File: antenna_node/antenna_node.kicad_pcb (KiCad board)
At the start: 4 copper layers, 68 parts, among them P1 CONN_01X03, P2 CONN_01X03, P3 CONN_01X02, P4 CONN_02X08, P5 CONN_01X06, P6 CONN_01X03, SW1 SW_PUSH, SW2 SW_PUSH, U1 0896BM15A0001, U2 TC77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

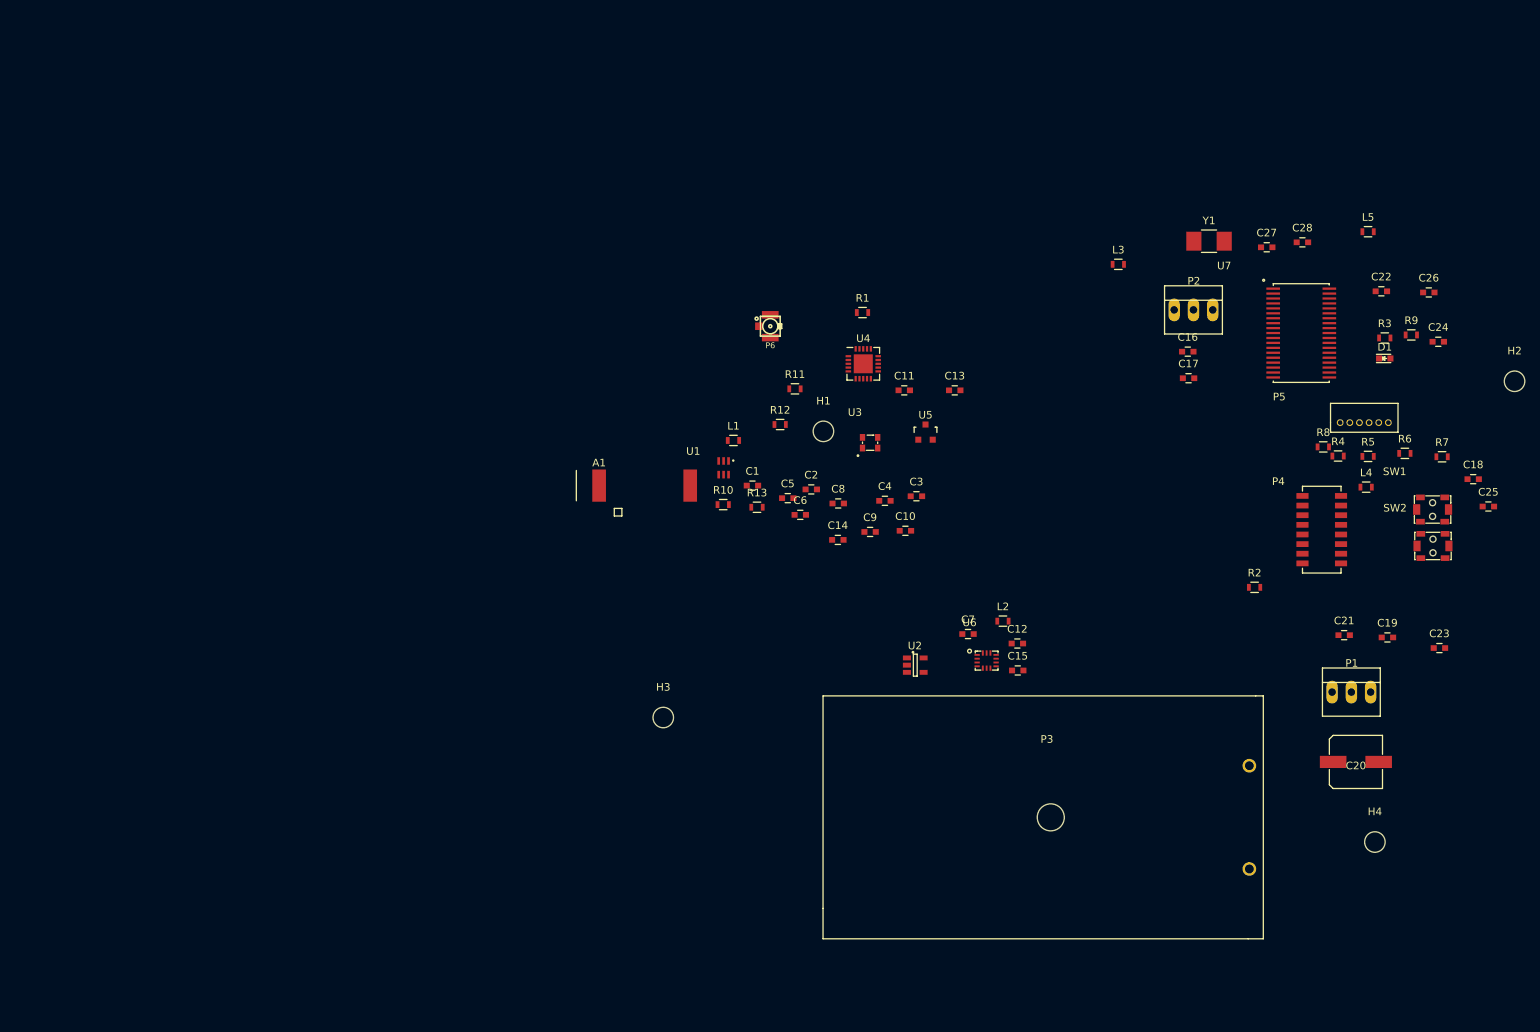
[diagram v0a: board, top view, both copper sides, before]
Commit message: finished initial compomnent placement, added rf shield and enclosure
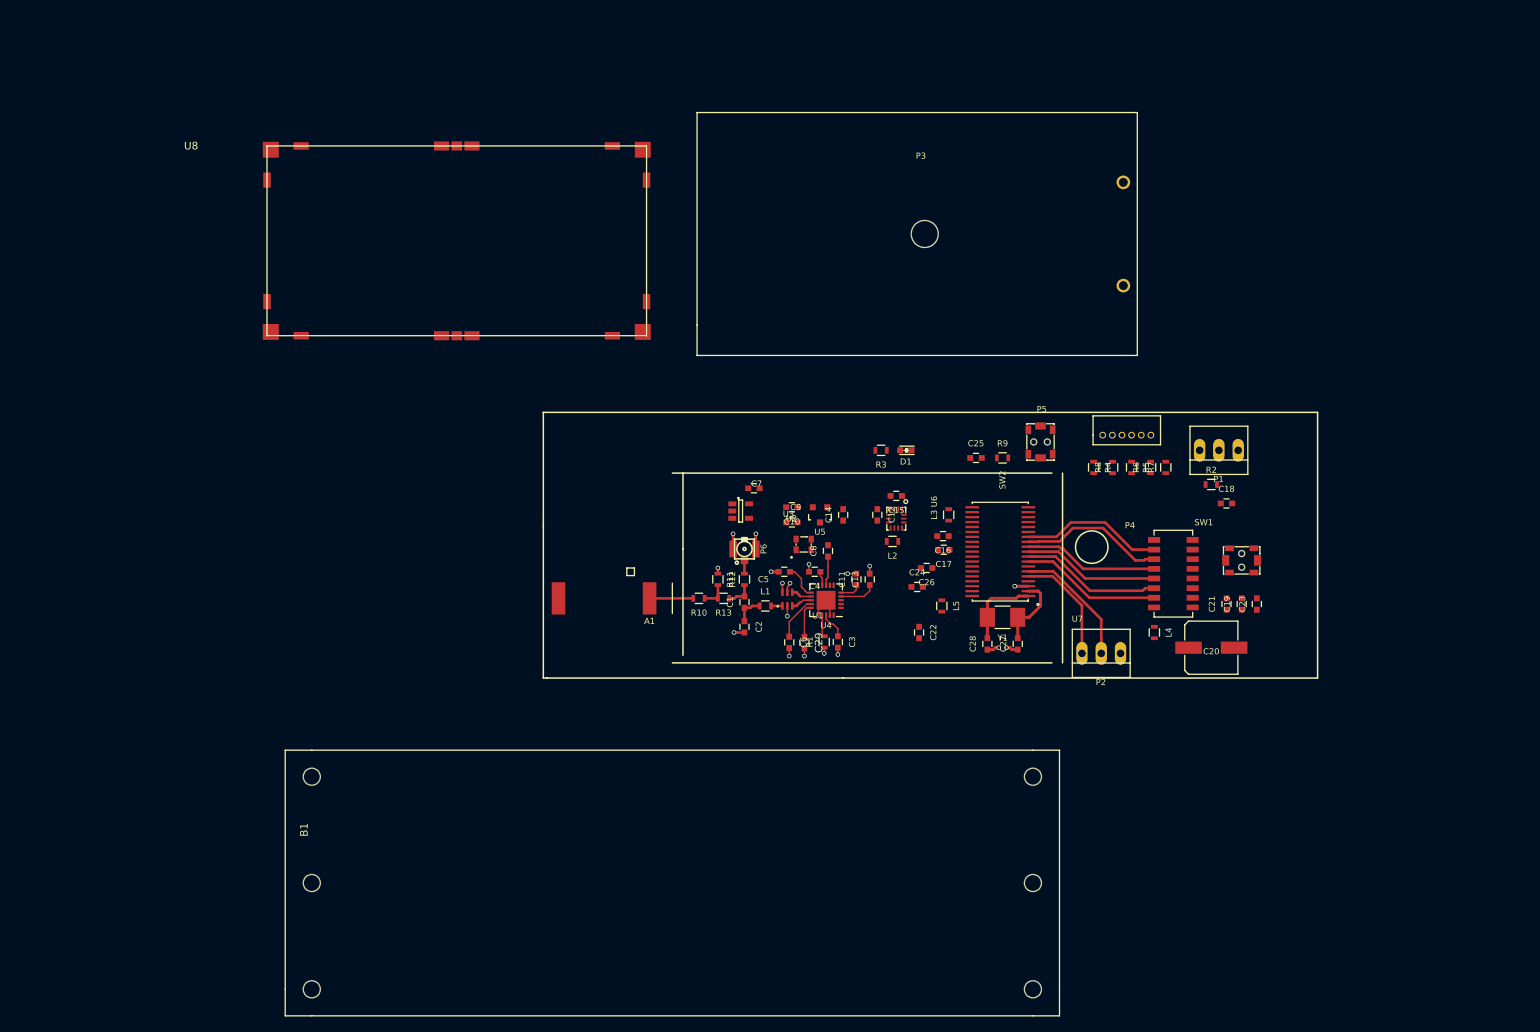
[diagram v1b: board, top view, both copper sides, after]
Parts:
- removed H1, H2, H3, H4: MOUNTING_HOLE, Mounting_Holes:MountingHole_2-7mm
- added B1: 1555C2F22GY, sensornode:1555CF22, F.Cu at (60.0, 146.0)
- added C29: 100 nF, Capacitors_SMD:C_0603, F.Cu at (124.9, 114.3)
- added U8: S01-50250500, sensornode:S01-50250500, F.Cu at (54.1, 73.9)
- C20: value 330 uF -> 220 uF
- P4: value CONN_02X08 -> DIL16
- moved P3 78.6 mm to (140.8, 60.5)
- moved C24 75.9 mm to (139.8, 107.0)
- moved C22 75.7 mm to (140.0, 113.0), turned to 270 degrees
- moved C26 75.5 mm to (141.0, 104.5), turned to 180 degrees
- moved L5 74.7 mm to (143.0, 109.5), turned to 270 degrees
- moved R3 68.0 mm to (135.0, 89.0), turned to 180 degrees
- moved C25 67.8 mm to (147.5, 90.0)
- moved C28 67.2 mm to (149.0, 114.5), turned to 90 degrees
- moved D1 64.2 mm to (138.3, 89.0), turned to 180 degrees
- moved C27 61.7 mm to (153.0, 114.5), turned to 90 degrees
- moved Y1 56.5 mm to (151.0, 111.0), turned to 180 degrees
- moved R9 56.2 mm to (151.0, 90.0)
- moved SW2 53.5 mm to (156.0, 87.9), turned to 90 degrees
- moved U7 47.5 mm to (150.7, 101.0), turned to 180 degrees
- moved P2 46.9 mm to (164.0, 115.8), turned to 180 degrees
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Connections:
- A1 pad 2: GND -> Net-(A1-Pad2)
- P4 pad 1: /SWADDR0 -> /SWDEBUG
- P4 pad 11: /SWADDR5 -> GND
- P4 pad 13: /SWDEBUG -> GND
- P4 pad 15: Net-(P1-Pad3) -> GND
- P4 pad 2: Net-(L4-Pad1) -> /SWADDR5
- P4 pad 3: /SWADDR1 -> /SWADDR4
- P4 pad 4: GND -> /SWADDR3
- P4 pad 6: GND -> /SWADDR1
- P4 pad 7: /SWADDR3 -> /SWADDR0
- P4 pad 8: GND -> Net-(L4-Pad1)
- P4 pad 9: /SWADDR4 -> Net-(P1-Pad3)
- R11 pad 1: Net-(R10-Pad1) -> Net-(C1-Pad2)
- U4 pad 6: Net-(U4-Pad6) -> /CC_GDO
- U7 pad 7: Net-(U7-Pad7) -> /CC_GDO
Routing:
- net GND: track 0.00 -> 26.0 mm, vias 0 -> 18
- net VCC: track 0.00 -> 25.3 mm
- net /SWADDR4: track 0.00 -> 19.1 mm
- net /SWADDR5: track 0.00 -> 18.8 mm
- net /SWADDR1: track 0.00 -> 18.6 mm
- net /SWADDR0: track 0.00 -> 18.5 mm
- net /SWADDR2: track 0.00 -> 18.0 mm
- net /SWADDR3: track 0.00 -> 17.8 mm
- net Net-(P2-Pad2): track 0.00 -> 16.7 mm
- net Net-(P2-Pad3): track 0.00 -> 14.9 mm
- net Net-(C28-Pad2): track 0.00 -> 10.5 mm
- net Net-(C27-Pad2): track 0.00 -> 9.75 mm
- net Net-(A1-Pad1): track 0.00 -> 5.75 mm
- net Net-(C8-Pad1): track 0.00 -> 3.89 mm
- net Net-(C1-Pad1): track 0.00 -> 3.85 mm
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- added copper zone on In1.Cu, net GND

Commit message: finished most of layout, silkscreen cleanup and DFM remains..
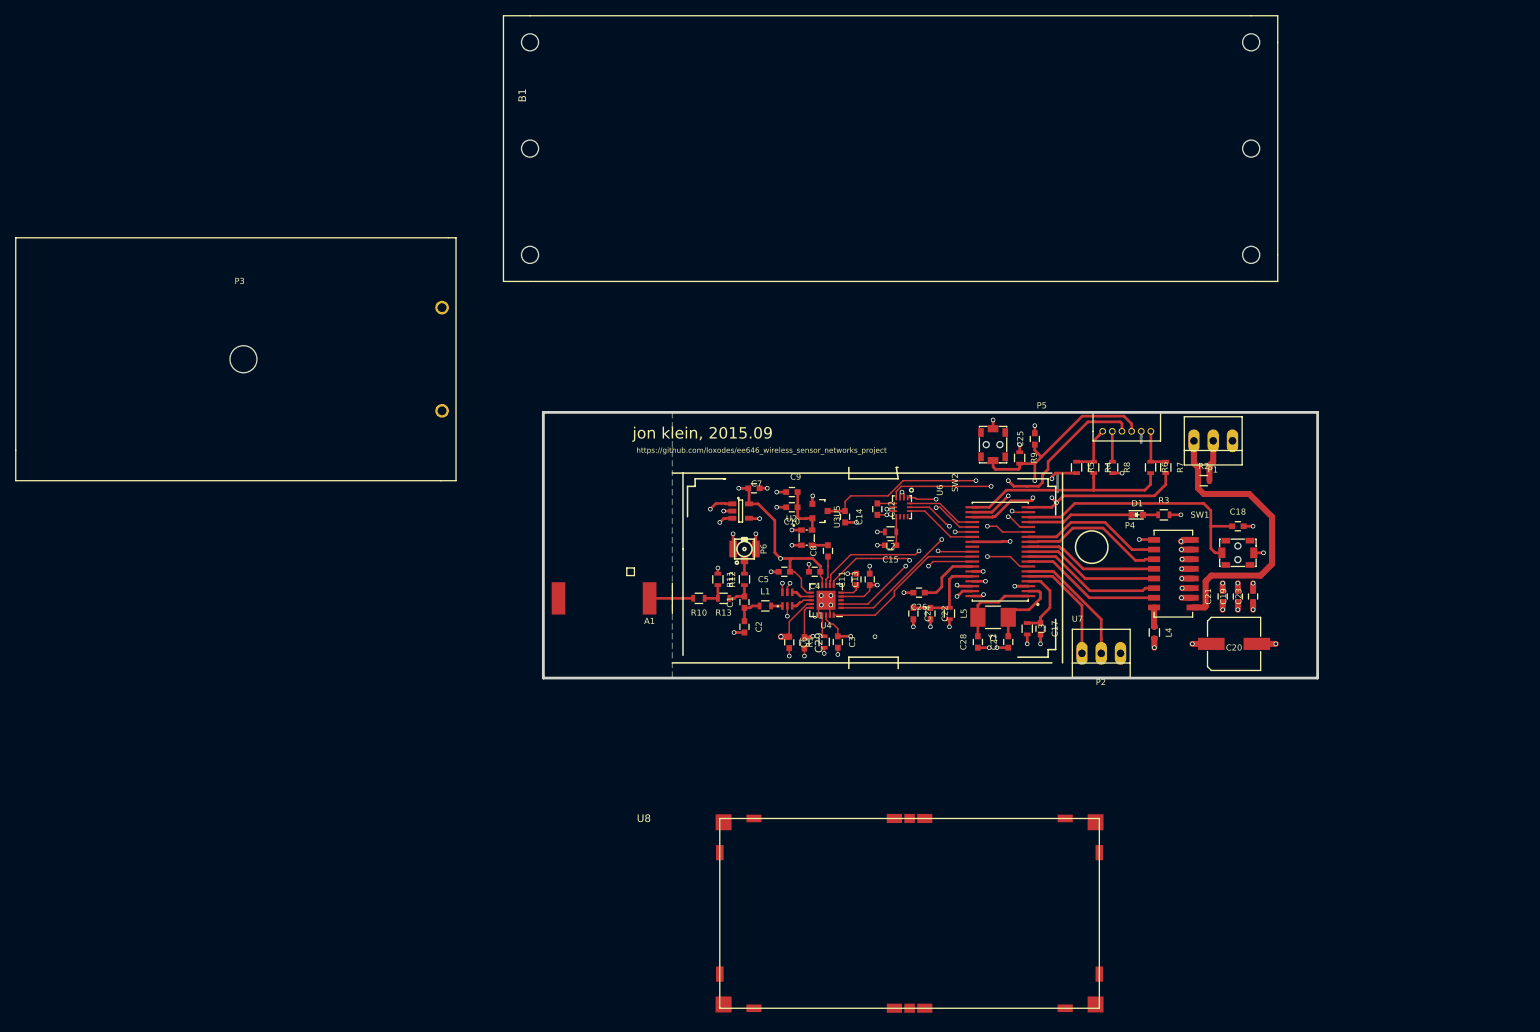
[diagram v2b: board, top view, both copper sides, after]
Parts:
- removed C16: 1000 nF, Capacitors_SMD:C_0603
- moved U8 106.8 mm to (113.8, 162.5)
- moved B1 100.9 mm to (88.8, 49.2)
- moved P3 91.3 mm to (51.0, 77.0)
- moved R3 38.2 mm to (172.2, 97.5), turned to 0 degrees
- moved D1 31.7 mm to (168.7, 97.5), turned to 0 degrees
- moved L3 18.2 mm to (154.2, 112.5), turned to 270 degrees
- moved C17 16.5 mm to (156.0, 112.5), turned to 270 degrees
- moved C25 8.14 mm to (155.2, 87.5), turned to 90 degrees
- moved R5 7.25 mm to (160.8, 91.2)
- moved C15 6.54 mm to (136.2, 101.5)
- moved SW2 6.26 mm to (149.8, 88.2)
- moved C9 4.00 mm to (123.2, 94.5)
- moved C24 3.54 mm to (139.2, 110.5), turned to 270 degrees
- moved C26 3.40 mm to (140.0, 107.8)
- moved C18 3.35 mm to (182.0, 99.0)
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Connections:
- U6 pad 12: (no net) -> /LSM_CS
- U6 pad 9: /LSM_INT2 -> Net-(U6-Pad9)
- U7 pad 14: /CC_SCLK -> /LSM_SCLK
- U7 pad 23: /CC_SI -> /LSM_MOSI
- U7 pad 24: /CC_SO -> /LSM_MISO
- U7 pad 25: /LSM_SCLK -> /CC_SCLK
- U7 pad 26: /CC_CSn -> /LSM_CS
- U7 pad 28: /LSM_INT2 -> Net-(U7-Pad28)
- U7 pad 29: /LSM_CS -> /CC_CSn
- U7 pad 30: /LSM_MOSI -> /CC_SI
- U7 pad 31: /LSM_MISO -> /CC_SO
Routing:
- net (no net): track 0.00 -> 276.5 mm
- net /TC_SIO: track 0.00 -> 73.3 mm, vias 0 -> 2
- net VCC: track 25.3 -> 95.8 mm, vias 0 -> 18
- net /TC_CS: track 0.00 -> 63.3 mm, vias 0 -> 2
- net /TC_SCK: track 0.00 -> 62.8 mm, vias 0 -> 2
- net GND: track 26.0 -> 77.5 mm, vias 18 -> 56
- net /RST: track 0.00 -> 39.7 mm, vias 0 -> 2
- net Net-(P1-Pad3): track 0.00 -> 38.8 mm
- net /AUXSW0: track 0.00 -> 34.7 mm
- net /XTAL_EN: track 0.00 -> 31.8 mm, vias 0 -> 2
- net /TST: track 0.00 -> 28.7 mm, vias 0 -> 2
- net /MCU_RXD: track 0.00 -> 28.5 mm
- net /CC_GDO: track 0.00 -> 28.3 mm, vias 0 -> 2
- net /MCU_TXD: track 0.00 -> 28.0 mm, vias 0 -> 3
- net /SWDEBUG: track 0.00 -> 25.6 mm, vias 0 -> 2
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- added copper zone on B.Cu, net GND
- added copper zone on In1.Cu, net VCC
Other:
- board outline added: 102 x 35 mm
- board text added: "https://github.com/loxodes/ee646_wireless_sensor_networks_project"
- board text added: "jon klein, 2015.09"

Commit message: finished cleanup, ordered r0
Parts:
- added Q1: Q_PMOS_GDS, Housings_SOT-23_SOT-143_TSOT-6:SOT-23_Handsoldering, F.Cu at (182.7, 95.5)
- P3: moved to B.Cu
- moved P3 114.4 mm to (162.6, 101.8)
- moved B1 52.6 mm to (94.0, 101.6)
- moved U8 45.7 mm to (109.0, 117.0)
- moved SW2 8.51 mm to (141.2, 87.8), turned to 180 degrees
- moved R9 8.08 mm to (145.8, 87.0)
- moved C25 6.77 mm to (148.5, 87.0)
- moved R2 1.30 mm to (178.0, 94.2), turned to 90 degrees
- moved C20 1.25 mm to (180.2, 114.5)
- moved P2 0.87 mm to (164.7, 115.2)
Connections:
- P4 pad 9: Net-(P1-Pad3) -> Net-(P4-Pad9)
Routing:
- net GND: track 77.5 -> 108.1 mm, vias 56 -> 75
- net Net-(P1-Pad3): track 38.8 -> 12.7 mm
- net Net-(P4-Pad9): track 0.00 -> 25.4 mm
- net Net-(P1-Pad2): track 5.46 -> 17.5 mm
- net VCC: track 95.8 -> 102.0 mm, vias 18 -> 17
- net /MCU_TXD: track 28.0 -> 23.8 mm, vias 3 -> 2
- net /MCU_RXD: track 28.5 -> 32.6 mm, vias 0 -> 2
- net /RST: track 39.7 -> 43.0 mm, vias 2 -> 0
- net (no net): track 276.5 -> 274.0 mm
- net /TST: track 28.7 -> 28.1 mm
- net /AUXSW0: track 34.7 -> 34.8 mm, vias 0 -> 2
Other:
- board text added: "ADDR0"
- board text added: "ADDR1"
- board text added: "ADDR2"
- board text added: "ADDR3"
- board text added: "ADDR4"
- board text added: "ADDR5"
- board text added: "AUX SW"
- board text added: "DBG"
- board text added: "GND"
- board text added: "LSM6DS3"
- board text added: "P1.0"
- board text added: "P1.1"
- board text added: "PWR"
- board text added: "RESET"
- board text added: "RST"
- board text added: "RXD"
- board text added: "TST"
- board text added: "TXD"
- board text added: "V+"
- board text added: "V+H"
- board text added: "V+L"
- board text added: "jon klein, 2015.09 r0"
- board text removed: "jon klein, 2015.09"

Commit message: started porting interrupt uart code, probably just not bother and just use busy wait version..
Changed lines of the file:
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@@
   )
   (setup
-    (last_trace_width 0.8)
+    (last_trace_width 0.16)
     (user_trace_width 0.2)
     (user_trace_width 0.36)
@@
     (pad_drill 0.762)
     (pad_to_mask_clearance 0.2)
+    (pad_to_paste_clearance -0.035)
     (aux_axis_origin 0 0)
     (visible_elements FFFEFF7F)
     (pcbplotparams
-      (layerselection 0x010f0_80000007)
+      (layerselection 0x010f8_80000007)
       (usegerberextensions false)
       (excludeedgelayer true)
@@
     (effects (font (size 0.6 0.6) (thickness 0.15)))
   )
-  (gr_text GND (at 167.25 111.25 360) (layer F.SilkS)
+  (gr_text GND (at 167.25 111.25) (layer F.SilkS)
     (effects (font (size 0.8 0.8) (thickness 0.15)))
   )
